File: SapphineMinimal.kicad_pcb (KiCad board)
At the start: 4 copper layers, 54.6 x 61 mm, 155 parts, among them IC201 DLHR-F50D-E1BD-C-NAV8, J301 503182-1852, J401 Conn_01x01_Male, J501 JST, J801 USB_B_Micro, J802 Conn_02x05_Odd_Even, J803 Conn_02x05_Odd_Even, J805 Conn_01x04_Male, M701 AdafruitWINC1500, Q501 BC857BS, Q502 IRLML6402TRPBF, SW601 EVQP7C01P, SW801 EVQP7C01P, U201 LIS331DLHTR, U202 BMP388, U301 MB85RS1MT, U302 TPS22860DBVR, U401 TPS22860DBVR, U402 SAM-M8Q-0-10, U501 TPS62150, U601 DS3231SN, U801 ATSAMD21G18A-A

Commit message: Working on update to power controllers
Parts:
- removed R403, R404, R405, R407, R408, R820, R821, R822, R823, R824, R825, R826, R827, R828, R829, R830, R831, R832, R833, R834, R835, R836, R837, R838, R839, R840: 47, Resistor_SMD:R_0603_1608Metric
- removed R409, R410: open, Resistor_SMD:R_0603_1608Metric
- added C303: 100nF, Capacitor_SMD:C_0603_1608Metric, F.Cu at (78.1, 37.5)
- added R813: EXB-2HV470JV, Sapphire:EXB-2HV470JV, F.Cu at (111.5, 94.1)
- added R814: EXB-2HV470JV, Sapphire:EXB-2HV470JV, F.Cu at (102.9, 84.7)
- R401, R809: value 47 -> EXB-2HV470JV; footprint Resistor_SMD:R_0603_1608Metric -> Sapphire:EXB-2HV470JV
- moved R301 169.7 mm to (81.9, 39.4)
- moved R303 169.6 mm to (81.9, 41.3)
- moved R304 169.6 mm to (81.9, 43.2)
- moved C301 169.0 mm to (103.5, 46.7)
- moved C302 169.0 mm to (103.3, 43.4)
- moved R302 169.0 mm to (95.1, 55.4)
- moved R305 169.0 mm to (99.4, 50.3)
- moved R306 169.0 mm to (99.9, 57.4)
- moved R307 169.0 mm to (94.4, 51.3)
- moved R308 169.0 mm to (99.7, 52.6)
- moved R309 169.0 mm to (99.7, 55.4)
- moved R310 169.0 mm to (99.7, 59.7)
- moved U301 169.0 mm to (76.5, 41.4)
- moved U302 169.0 mm to (91.1, 56.6)
- moved U202 133.8 mm to (129.5, 74.4)
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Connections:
- net /Sapphire_Proc/AREF renamed /Sapphire_Proc/PA03
- net /Sapphire_Proc/GNSS_PWR renamed /Sapphire_Proc/PA11
- net /Sapphire_Proc/SD_CS renamed /Sapphire_Proc/PA08
- net /Sapphire_Proc/SD_PWR renamed /Sapphire_Proc/PA10
- net Net-(C803-Pad2) renamed /Sapphire_Proc/RESET_PIN
- FB402 pad 1: Net-(FB402-Pad1) -> /Sapphire_Proc/RS232_RXD5
- FB403 pad 1: Net-(FB403-Pad1) -> /Sapphire_Proc/RS232_TXD5
- IC201 pad 5: /Sapphire_Proc/DLHR_EOC -> /Sapphire_Proc/PA18
- R401 pad 1: /Sapphire_Proc/TIMEMARK -> /P3V3
- R401 pad 2: Net-(R401-Pad2) -> /Sapphire_Proc/PA14
- R604 pad 2: /Sapphire_Proc/LOCAL_PPS -> /Sapphire_Proc/PA28
- R809 pad 1: /Sapphire_Proc/SWDIO -> /Sapphire_Proc/PB1
- R809 pad 2: /SapphireMini_SD/FRAM_WP -> /Sapphire_Proc/ACC_INT1
- R812 pad 10: /Sapphire_Proc/PA09 -> /Sapphire_Proc/PA06
- R812 pad 11: /Sapphire_Proc/PA07 -> /Sapphire_Proc/PA05
- R812 pad 12: /Sapphire_Proc/PA06 -> /Sapphire_Proc/PA04
- R812 pad 13: /Sapphire_Proc/PA05 -> /Sapphire_Proc/PB09
- R812 pad 14: /Sapphire_Proc/PA04 -> /Sapphire_Proc/PB08
- R812 pad 3: unconnected-(R812-Pad3) -> /Sapphire_Proc/WIFI_RESET
- R812 pad 4: /SapphireMini_Power/VBAT_MON -> /Sapphire_Proc/WIFI_IRQ
- R812 pad 9: /Sapphire_Proc/PA12 -> /Sapphire_Proc/PA07
- U402 pad 12: Net-(R409-Pad1) -> /SapphireMini_GNSS/SAM_SCL
- U402 pad 13: Net-(FB402-Pad2) -> /SapphireMini_GNSS/SAM_TXD
- U402 pad 14: Net-(FB403-Pad2) -> /SapphireMini_GNSS/SAM_RXD
- U402 pad 18: Net-(R407-Pad1) -> /SapphireMini_GNSS/SAM_RESET
- U402 pad 19: Net-(R408-Pad1) -> /SapphireMini_GNSS/SAM_EXTINTO
- U402 pad 3: Net-(R405-Pad2) -> /SapphireMini_GNSS/V_BCKP
- U402 pad 7: Net-(R401-Pad2) -> /SapphireMini_GNSS/TIMEPULSE
- U402 pad 9: Net-(R410-Pad1) -> /SapphireMini_GNSS/SAM_SDA
- U601 pad 3: /Sapphire_Proc/LOCAL_PPS -> /Sapphire_Proc/PA28
- U801 pad 19: Net-(R837-Pad2) -> /Sapphire_Proc/PB10
- U801 pad 20: Net-(R838-Pad2) -> /Sapphire_Proc/PB11
- U801 pad 21: unconnected-(U801-Pad21) -> /Sapphire_Proc/PA12
- U801 pad 22: Net-(R820-Pad1) -> /Sapphire_Proc/PA13
- U801 pad 23: Net-(R821-Pad1) -> /Sapphire_Proc/PA14
- U801 pad 24: Net-(R822-Pad1) -> /Sapphire_Proc/PA15
- U801 pad 27: Net-(R823-Pad1) -> /Sapphire_Proc/PA18
- U801 pad 28: Net-(R824-Pad1) -> /SapphireMini_SD/SPI_MISO
- U801 pad 29: Net-(R825-Pad1) -> /Sapphire_Proc/PA20
- U801 pad 30: Net-(R826-Pad1) -> /Sapphire_Proc/PA21
- U801 pad 31: Net-(R827-Pad1) -> /SapphireMini_DLHR/I2C_SDA
- U801 pad 32: Net-(R828-Pad1) -> /SapphireMini_DLHR/I2C_SCL
- U801 pad 33: Net-(R829-Pad1) -> /Sapphire_Proc/PA24
- U801 pad 34: Net-(R830-Pad1) -> /Sapphire_Proc/PA25
- U801 pad 37: Net-(R839-Pad2) -> /Sapphire_Proc/PB22
- U801 pad 38: Net-(R840-Pad2) -> /Sapphire_Proc/PB23
- U801 pad 39: Net-(R831-Pad1) -> /Sapphire_Proc/PA27
- U801 pad 41: Net-(R832-Pad1) -> /Sapphire_Proc/PA28
- U801 pad 47: Net-(R833-Pad2) -> /Sapphire_Proc/PB02
- U801 pad 48: Net-(R834-Pad2) -> /Sapphire_Proc/PB03
- U801 pad 7: Net-(R835-Pad2) -> /Sapphire_Proc/PB08
- U801 pad 8: Net-(R836-Pad2) -> /Sapphire_Proc/PB09
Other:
- outline, holes or cut-outs redrawn

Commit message: Checkpoint
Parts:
- removed C204, C402: 10uF, Capacitor_SMD:C_0805_2012Metric
- removed C206: 100nF, Capacitor_SMD:C_0603_1608Metric
- removed C301, C403: 22uF, Capacitor_SMD:C_1206_3216Metric
- removed FB401: FerriteBead, Inductor_SMD:L_0201_0603Metric
- removed R202, R203, R207, R208, R209, R210: 47, Resistor_SMD:R_0603_1608Metric
- removed R302, R406: 100K, Resistor_SMD:R_0603_1608Metric
- removed R402: 0R25, Resistor_SMD:R_0603_1608Metric
- removed U302, U401: TPS22860DBVR, SapphineMinimal:SOT95P280X145-6N
- added C506: 10uF, Capacitor_SMD:C_0805_2012Metric, F.Cu at (95.9, 114.3)
- added C507: 10uF, Capacitor_SMD:C_0805_2012Metric, F.Cu at (95.9, 111.8)
- added C508: 10uF, Capacitor_SMD:C_0805_2012Metric, F.Cu at (100.3, 116.2)
- added C509: 100nF, Capacitor_SMD:C_0603_1608Metric, F.Cu at (103.3, 112.8)
- added C510: 10uF, Capacitor_SMD:C_0805_2012Metric, F.Cu at (100.3, 108.9)
- added IC501: SLG59M1446V, SamacSys_Parts:SLG59M1446V, F.Cu at (99.8, 112.5)
- added R512: 100K, Resistor_SMD:R_0603_1608Metric, F.Cu at (95.7, 108.0)
- added R513: 100K, Resistor_SMD:R_0603_1608Metric, F.Cu at (96.1, 118.7)
- added R514: 20K0, Resistor_SMD:R_0603_1608Metric, F.Cu at (95.9, 109.9)
- added R515: 20K0, Resistor_SMD:R_0603_1608Metric, F.Cu at (96.1, 116.8)
- C302, C401, J401, J805, R305, R306, R307, R308, R309: moved to B.Cu
- R201: value 47 -> EXB-2HV470JV; footprint Resistor_SMD:R_0603_1608Metric -> Sapphire:EXB-2HV470JV
- R812: footprint SapphineMinimal:EXB-2HV470JV -> Sapphire:EXB-2HV470JV
- SW601, SW801: footprint SapphineMinimal:EVQP7C01P -> Sapphire:EVQP7C01P
- U201: footprint SapphineMinimal:LIS331DLHTR -> Sapphire:LIS331DLHTR
- moved R802 99.1 mm to (81.9, 104.8), turned to 90 degrees
- moved J802 83.0 mm to (83.8, 87.0), turned to -90 degrees
- moved R841 80.4 mm to (83.6, 91.6), turned to 90 degrees
- moved C810 74.2 mm to (87.0, 85.7)
- moved R502 71.6 mm to (84.2, 104.8)
- moved R503 71.6 mm to (87.5, 104.8)
- moved R504 71.6 mm to (90.8, 104.8)
- moved J805 69.5 mm to (128.3, 103.5), turned to -90 degrees
- moved S501 66.1 mm to (87.0, 109.2)
- moved J803 63.9 mm to (128.3, 108.0)
- moved J501 63.3 mm to (126.4, 122.6), turned to -90 degrees
- moved R508 62.7 mm to (120.1, 119.9)
- moved L501 61.4 mm to (127.1, 118.7)
- moved C504 61.4 mm to (119.0, 113.4)
- moved C505 61.4 mm to (122.8, 109.0)
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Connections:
- net /SapphireMini_GNSS/GNSS_POWER_OUT renamed /SapphireMini_GNSS/GNSS_OUTPUT_POWER
- net /Sapphire_Proc/PA08 renamed /SapphireMini_SD/SD_CS
- net Net-(C301-Pad1) renamed /SapphireMini_Power/SD_OUTPUT_POWER
- C803 pad 1: P3V3 -> /P3V3
- C810 pad 1: P3V3 -> /P3V3
- CR801 pad 1: Net-(CR801-Pad1) -> /Sapphire_Proc/D-
- CR801 pad 6: Net-(CR801-Pad6) -> /Sapphire_Proc/D+
- FB801 pad 1: P3V3 -> /P3V3
- IC201 pad 5: /Sapphire_Proc/PA18 -> /SapphireMini_DLHR/DLHR_EOC
- J301 pad 3: /SapphireMini_SD/SPI_MOSI -> Net-(J301-Pad3)
- J301 pad 5: /SapphireMini_SD/SPI_SCK -> Net-(J301-Pad5)
- J301 pad SW: /Sapphire_Proc/SD_CD -> GND
- J801 pad 2: Net-(CR801-Pad1) -> /Sapphire_Proc/D-
- J801 pad 3: Net-(CR801-Pad6) -> /Sapphire_Proc/D+
- J802 pad 1: P3V3 -> /P3V3
- J805 pad 2: P3V3 -> /P3V3
- L701 pad 1: /Sapphire_WiFi/P3V3 -> /P3V3
- L801 pad 1: P3V3 -> /P3V3
- R201 pad 1: Net-(R201-Pad1) -> /SapphireMini_DLHR/I2C_SCL
- R201 pad 2: /SapphireMini_DLHR/I2C_SCL -> GND
- R308 pad 1: /SapphireMini_SD/SPI_MOSI -> Net-(J301-Pad3)
- R309 pad 1: /SapphireMini_SD/SPI_SCK -> Net-(J301-Pad5)
- R310 pad 1: GND -> /Sapphire_Proc/SD_CD
- R401 pad 10: /SapphireMini_GNSS/SAM_RESET -> /SapphireMini_GNSS/SAM_EXTINTO
- R401 pad 14: /SapphireMini_GNSS/SAM_SDA -> /SapphireMini_GNSS/TIMEPULSE
- R401 pad 15: /SapphireMini_GNSS/TIMEPULSE -> /SapphireMini_GNSS/SAM_SDA
- R401 pad 2: /Sapphire_Proc/PA14 -> /SapphireMini_DLHR/I2C_SDA
- R401 pad 3: /SapphireMini_DLHR/I2C_SDA -> /Sapphire_Proc/TIMEMARK
- R401 pad 7: /SapphireMini_GNSS/GNSS_RESET -> /Sapphire_Proc/GNSS_EXTINT
- R401 pad 8: /Sapphire_Proc/GNSS_EXTINT -> /SapphireMini_GNSS/GNSS_RESET
- R401 pad 9: /SapphireMini_GNSS/SAM_EXTINTO -> /SapphireMini_GNSS/SAM_RESET
- R604 pad 2: /Sapphire_Proc/PA28 -> /SapphireMini_DS3231/SQW
- R802 pad 1: P3V3 -> /P3V3
- R807 pad 1: P3V3 -> /P3V3
- R808 pad 1: P3V3 -> /P3V3
- R809 pad 6: /Sapphire_Proc/PA14 -> /Sapphire_Proc/TIMEMARK
- R809 pad 8: /Sapphire_Proc/PA18 -> /SapphireMini_DLHR/DLHR_EOC
- R811 pad 2: P3V3 -> /P3V3
- R813 pad 12: /SapphireMini_DLHR/I2C_SCL -> /Sapphire_Proc/PA23
- R813 pad 13: /SapphireMini_DLHR/I2C_SDA -> /Sapphire_Proc/PA22
- R813 pad 16: /SapphireMini_SD/SPI_MISO -> /Sapphire_Proc/PA19
- R813 pad 7: unconnected-(R813-Pad7) -> /Sapphire_Proc/D+
- R814 pad 4: /Sapphire_Proc/PA28 -> /SapphireMini_DS3231/SQW
- R841 pad 1: P3V3 -> /P3V3
- R842 pad 2: P3V3 -> /P3V3
- U201 pad 11: Net-(R207-Pad2) -> Net-(R201-Pad12)
- U201 pad 4: Net-(R201-Pad1) -> Net-(R201-Pad16)
- U201 pad 6: Net-(R202-Pad1) -> Net-(R201-Pad14)
- U201 pad 7: Net-(R203-Pad1) -> Net-(R201-Pad15)
- U201 pad 9: Net-(R208-Pad2) -> Net-(R201-Pad13)
- U202 pad 2: Net-(R209-Pad1) -> /SapphireMini_DLHR/BMP_SCK
- U202 pad 4: Net-(R210-Pad1) -> /SapphireMini_DLHR/BMP_SDI
- U601 pad 3: /Sapphire_Proc/PA28 -> /SapphireMini_DS3231/SQW
- U801 pad 15: /Sapphire_Proc/PA10 -> /SapphireMini_Power/SD_PWR
- U801 pad 16: /Sapphire_Proc/PA11 -> /SapphireMini_Power/GNSS_PWR
- U801 pad 28: /SapphireMini_SD/SPI_MISO -> /Sapphire_Proc/PA19
- U801 pad 31: /SapphireMini_DLHR/I2C_SDA -> /Sapphire_Proc/PA22
- U801 pad 32: /SapphireMini_DLHR/I2C_SCL -> /Sapphire_Proc/PA23
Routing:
- net /P3V3: track 0.00 -> 297.8 mm, vias 0 -> 20
- net /Sapphire_Proc/D+: track 0.00 -> 35.0 mm, vias 0 -> 2
- net /Sapphire_Proc/D-: track 0.00 -> 34.4 mm, vias 0 -> 2
- net /SapphireMini_Power/PWR_IN: track 0.00 -> 19.9 mm, vias 0 -> 2
- net /SapphireMini_GNSS/TIMEPULSE: track 0.00 -> 18.3 mm
- net Net-(C801-Pad1): track 0.00 -> 16.6 mm
- net /SapphireMini_Power/SD_OUTPUT_POWER: track 0.00 -> 15.7 mm, vias 0 -> 1
- net /SapphireMini_GNSS/SAM_EXTINTO: track 0.00 -> 15.4 mm
- net /SapphireMini_GNSS/SAM_SDA: track 0.00 -> 13.4 mm
- net /SapphireMini_Power/VBAT: track 0.00 -> 13.1 mm
- net /SapphireMini_GNSS/SAM_RESET: track 0.00 -> 12.7 mm
- net /Sapphire_Proc/PA00: track 0.00 -> 12.2 mm, vias 0 -> 2
- net /Sapphire_Proc/PA02: track 0.00 -> 10.5 mm, vias 0 -> 2
- net Net-(D501-Pad1): track 0.00 -> 8.25 mm
- net /SapphireMini_Power/VBUS: track 0.00 -> 7.88 mm
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- added copper zone on B.Cu, net GND
- added copper zone on F.Cu, net GND
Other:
- outline, holes or cut-outs redrawn

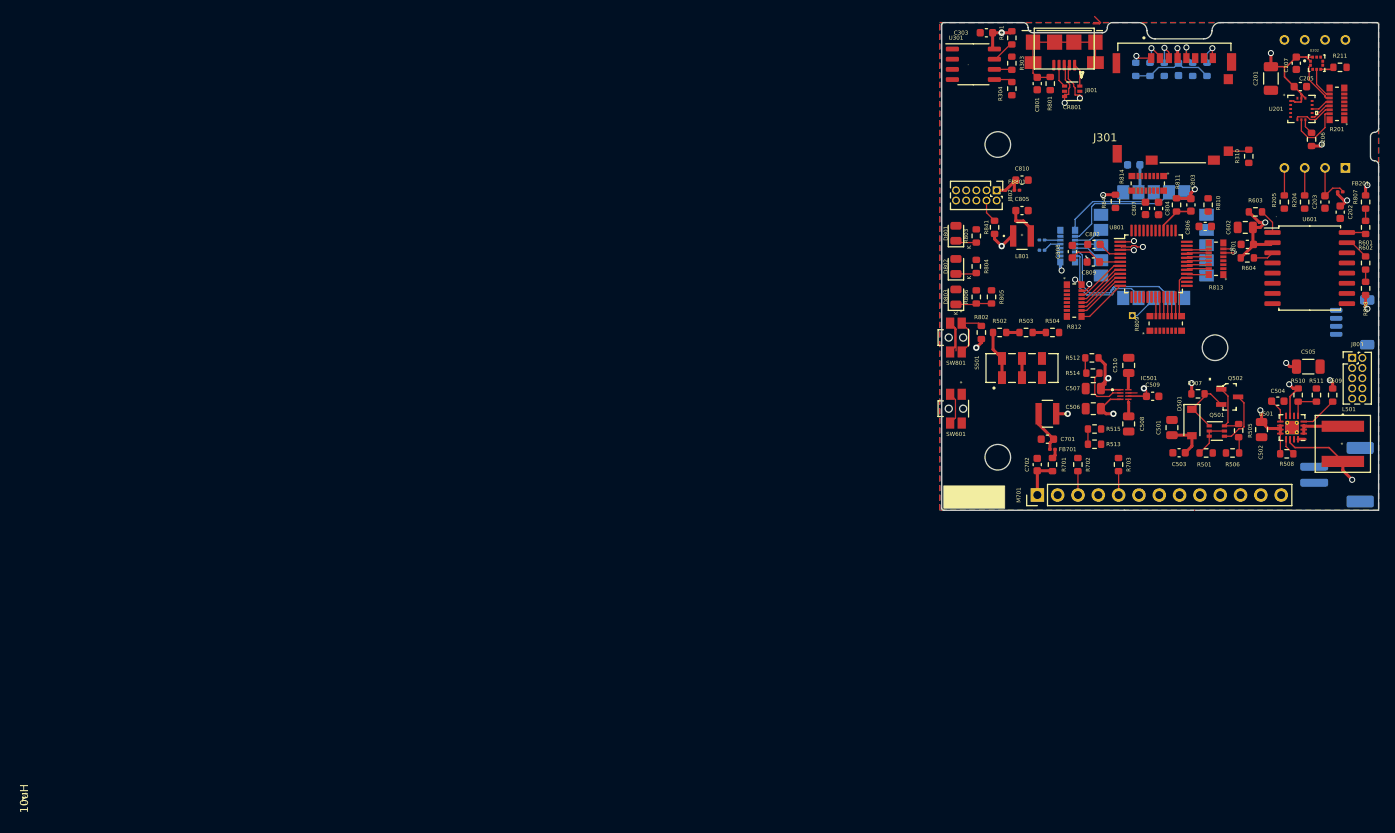
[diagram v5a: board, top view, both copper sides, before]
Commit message: Fully routed. Needs DRC check and cleanup
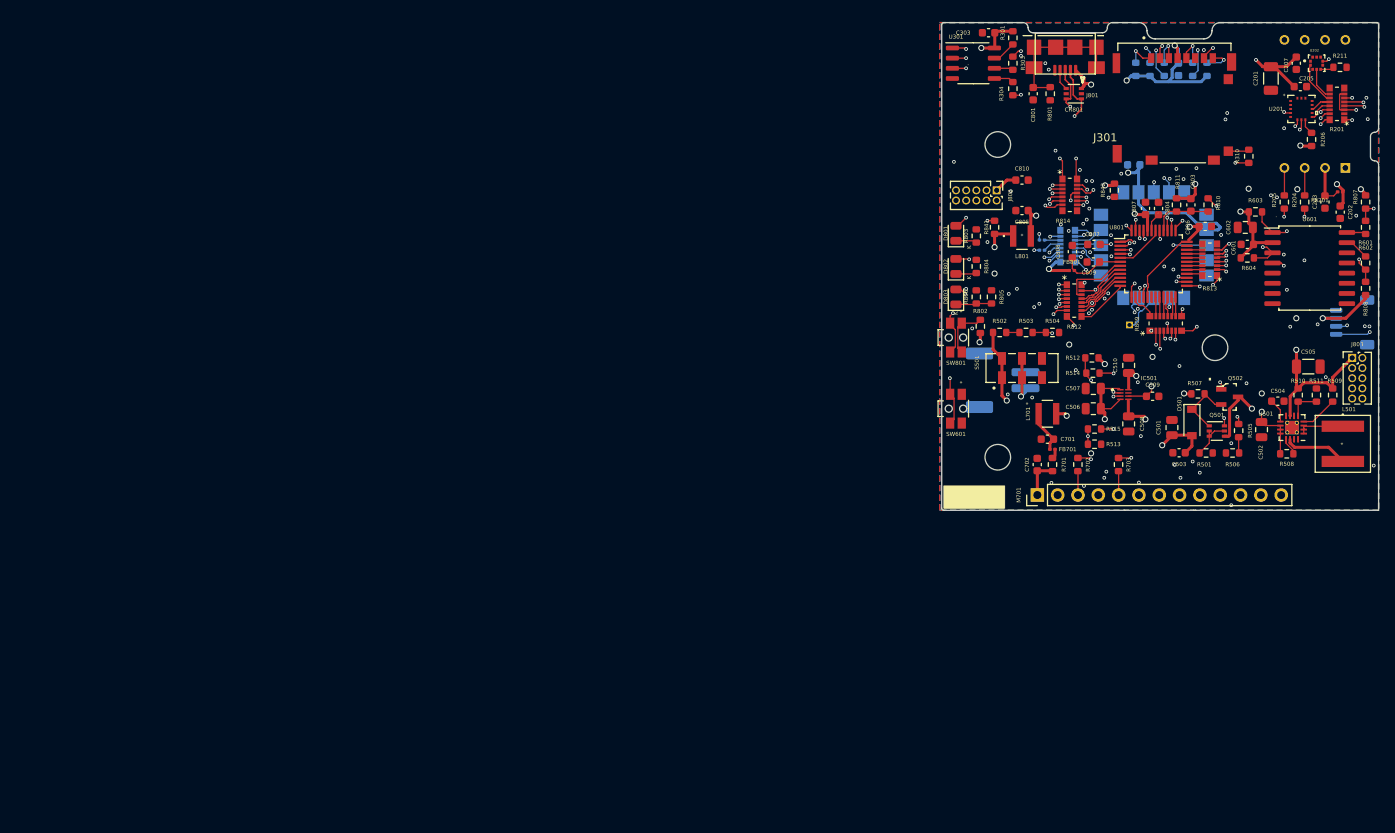
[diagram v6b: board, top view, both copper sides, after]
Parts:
- moved J501 43.4 mm to (84.6, 110.7), turned to 90 degrees
- moved FB801 12.2 mm to (93.2, 97.0)
- moved R814 9.86 mm to (93.0, 87.6), turned to 0 degrees
- moved R842 1.39 mm to (98.6, 87.0)
- moved C801 1.37 mm to (88.4, 74.9)
- moved R801 1.27 mm to (90.5, 74.9)
- moved J401 1.22 mm to (100.4, 103.8)
- moved R813 0.79 mm to (110.5, 95.7)
- moved R802 0.77 mm to (81.8, 104.0)
- moved J801 0.65 mm to (92.4, 69.1)
- moved CR801 0.37 mm to (93.5, 74.9)
- moved C303 0.27 mm to (82.8, 67.3)
- moved U301 0.13 mm to (80.9, 71.1)
- moved R301 0.13 mm to (85.9, 67.9)
- moved R303 0.13 mm to (85.9, 71.1)
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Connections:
- J803 pad 1: /Sapphire_Proc/PA12 -> /P3V3
- J803 pad 10: /Sapphire_Proc/PB23 -> /Sapphire_Proc/GREEN_LED
- J803 pad 2: /Sapphire_Proc/PA13 -> GND
- J803 pad 3: /Sapphire_Proc/PA20 -> /Sapphire_Proc/AUX1
- J803 pad 4: /Sapphire_Proc/PA21 -> /SapphireMini_SD/SPI_SCK
- J803 pad 5: /Sapphire_Proc/PB08 -> /Sapphire_Proc/AUX2
- J803 pad 6: /Sapphire_Proc/PB09 -> /SapphireMini_SD/SPI_MOSI
- J803 pad 7: /Sapphire_Proc/PB10 -> /Sapphire_Proc/AUX3
- J803 pad 8: /Sapphire_Proc/PB11 -> /SapphireMini_SD/SPI_MISO
- J803 pad 9: /Sapphire_Proc/PB22 -> /Sapphire_Proc/RED_LED
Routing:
- net /SapphireMini_SD/SPI_MISO: track 0.00 -> 136.0 mm, vias 0 -> 5
- net /SapphireMini_SD/SPI_MOSI: track 0.00 -> 131.5 mm, vias 0 -> 8
- net /SapphireMini_SD/SPI_SCK: track 0.00 -> 123.4 mm, vias 0 -> 8
- net /SapphireMini_DLHR/I2C_SCL: track 1.53 -> 93.3 mm, vias 0 -> 10
- net /SapphireMini_DLHR/I2C_SDA: track 1.52 -> 86.2 mm, vias 0 -> 8
- net /Sapphire_Proc/GREEN_LED: track 0.00 -> 84.1 mm, vias 0 -> 5
- net /Sapphire_Proc/RED_LED: track 0.00 -> 78.1 mm, vias 0 -> 5
- net /Sapphire_Proc/RESET: track 4.15 -> 82.2 mm, vias 0 -> 4
- net /Sapphire_Proc/ACC_INT2: track 0.00 -> 59.9 mm, vias 0 -> 3
- net /Sapphire_Proc/ACC_INT1: track 0.00 -> 59.6 mm, vias 0 -> 3
- net /SapphireMini_Power/VBUS: track 7.88 -> 66.9 mm, vias 0 -> 3
- net /SapphireMini_DLHR/BMP_INT: track 0.00 -> 56.7 mm, vias 0 -> 3
- net /Sapphire_Proc/WIFI_EN: track 0.00 -> 54.8 mm, vias 0 -> 2
- net /Sapphire_Proc/WIFI_CS: track 0.00 -> 51.7 mm, vias 0 -> 3
- net /SapphireMini_GNSS/GNSS_OUTPUT_POWER: track 5.85 -> 57.0 mm, vias 0 -> 2
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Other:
- outline, holes or cut-outs redrawn
